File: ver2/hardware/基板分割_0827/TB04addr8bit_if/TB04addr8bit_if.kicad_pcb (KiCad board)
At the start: 2 copper layers, 295 x 195 mm, 307 parts, among them IC201 74HC161N, IC202 74HC161N, IC203 74HC161N, IC204 74HC161N, IC301 74HC161N, IC302 74HC161N, IC303 74HC161N, IC304 74HC161N, IC401 74HC161N, IC402 74HC161N, IC601 74HC161N, J1001 Conn_01x06_Socket, J1002 Conn_01x06_Socket, J1003 Conn_01x06_Socket, J1004 Conn_01x06_Socket, J101 USB_C_Receptacle_PowerOnly_6P, J601 Conn_02x05_Odd_Even, J801 Conn_02x05_Odd_Even, J802 Conn_02x05_Odd_Even, J803 Conn_02x05_Odd_Even, J804 Conn_02x05_Odd_Even, J805 Conn_02x05_Odd_Even, J806 Conn_02x05_Odd_Even, J807 Conn_02x05_Odd_Even, J808 Conn_02x05_Odd_Even, J901 Conn_02x05_Odd_Even, J902 Conn_02x05_Odd_Even, J903 Conn_02x05_Odd_Even, J904 Conn_02x05_Odd_Even, SW1001 SW_DIP_x04, SW1002 SW_DIP_x04, SW1003 SW_DIP_x04, SW1004 SW_DIP_x04, SW101 SW_SPDT, SW501 SW_Push, SW502 sw rotary, SW503 SW_Push, SW601 SW_Coded_SH-7050, U1001 74HC244, U1002 74HC244, U1003 74HC244, U1004 74HC244, U101 74LS157, U102 74HC138, U1101 6116, U1102 74HC244, U1103 74HC244, U1201 74HC193, U1301 74LS08, U1401 74HC138, U1402 74HC244, U1403 74HC244, U1404 74HC244, U1405 74HC244, U1406 74LS157, U1407 74LS139, U1501 74AHC04, U1503 74LS08, U1504 74HC00, U1505 74LS00, U1506 74LS32, U1507 74LS08, U1509 74LS10, U201 74LS253, U202 74LS253, U203 74LS253, U204 74LS253, U301 74LS253, U302 74LS253, U303 74LS253, U304 74LS253, U401 74LS157, U402 74LS253, U403 74LS253, U404 74LS157, U405 74LS253, U406 74LS253, U501 74HC14, U502 4060, U601 74LS273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

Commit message: ver2: 3分割のフットプリント設定完了・取付穴を追加・PCBを作り直し
- 新規コネクタ11件のフットプリントを設定(2x20/2x10ピンソケット・端子台)
- 演算板/制御板/キャリアに取付穴MountingHole_Pad×4とGNDを追加(M3・パッド付きビア)
- 3枚のPCBをコピー元マスターのレイアウトを一掃して作り直し(配置前・配線0)
- 階層から外れて残っていたRS00/RS01.kicad_sch(制御板・IF板)を削除

検証: フットプリント未設定0件、回路図とPCBの参照番号の集合差分0
(演算102/制御101/IF127/キャリア14)、回路図の電気的変更なし

Co-Authored-By: Claude Opus 5 <noreply@anthropic.com>
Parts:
- removed C101, C102, C1101, C1102, C1103, C1201, C1301, C1401, C1402, C1403, C1404, C1407, C1408, C1409, C1501, C1502, C1503, C1504, C1505, C1506, C1507, C201, C202, C203, C204, C205, C206, C207, C208, C301, C302, C303, C304, C305, C306, C307, C308, C401, C402, C403, C404, C405, C406, C407, C408, C601, C602, C603, C604, C605, C606, C607, C608, C701, C702, C703, C704, C705, C706: 0.1u, Capacitor_THT:C_Disc_D4.3mm_W1.9mm_P5.00mm
- removed D1201, D1202, D1203, D201, D202, D203, D204, D205, D206, D207, D208, D209, D210, D211, D212, D213, D214, D215, D216, D301, D302, D303, D304, D305, D306, D307, D308, D309, D310, D311, D312, D313, D314, D315, D316, D601, D602, D603, D604, D605, D606: LED, LED_THT:LED_D3.0mm_Clear
- removed IC201, IC202, IC203, IC204, IC301, IC302, IC303, IC304, IC401, IC402, IC601: 74HC161N, Package_DIP:DIP-16_W7.62mm_Socket
- removed J601, J801, J802, J803, J804, J805, J806, J807, J808: Conn_02x05_Odd_Even, Connector_PinSocket_2.54mm:PinSocket_2x05_P2.54mm_Vertical
- removed R1201, R1202, R1203: 4.7K, Resistor_THT:R_Axial_DIN0207_L6.3mm_D2.5mm_P10.16mm_Horizontal
- removed R601, R602: 3.3K, Resistor_THT:R_Axial_DIN0207_L6.3mm_D2.5mm_P7.62mm_Horizontal
- removed R603, R604, R605, R606: 10K, Resistor_THT:R_Axial_DIN0207_L6.3mm_D2.5mm_P10.16mm_Horizontal
- removed RN201, RN202, RN301, RN302: 4.7K, Resistor_THT:R_Array_SIP9
- removed RN601: 4.7K, Resistor_THT:R_Array_SIP5
- removed SW601: SW_Coded_SH-7050, Library:dip_rotary_sw
- removed U101, U1406, U401, U404: 74LS157, Package_DIP:DIP-16_W7.62mm_Socket
- removed U102, U1401: 74HC138, Package_DIP:DIP-16_W7.62mm_Socket
- removed U1101: 6116, Package_DIP:DIP-24_18.0mmx34.29mm_W15.24mm_Socket
- removed U1102, U1103, U1402, U1403, U1404, U1405: 74HC244, Package_DIP:DIP-20_W7.62mm_Socket
- removed U1201: 74HC193, Package_DIP:DIP-16_W7.62mm_Socket
- removed U1301, U1503, U1507: 74LS08, Package_DIP:DIP-14_W7.62mm_Socket
- removed U1407: 74LS139, Package_DIP:DIP-16_W7.62mm_Socket
- removed U1501: 74AHC04, Package_DIP:DIP-14_W7.62mm_Socket
- removed U1504: 74HC00, Package_DIP:DIP-14_W7.62mm_Socket
- removed U1505: 74LS00, Package_DIP:DIP-14_W7.62mm_Socket
- removed U1506: 74LS32, Package_DIP:DIP-14_W7.62mm_Socket
- removed U1509: 74LS10, Package_DIP:DIP-14_W7.62mm_Socket
- removed U201, U202, U203, U204, U301, U302, U303, U304, U402, U403, U405, U406: 74LS253, Package_DIP:DIP-16_W7.62mm_Socket
- removed U601, U701, U702, U705: 74LS273, Package_DIP:DIP-20_W7.62mm_Socket
- removed U602, U606: 74HC273, Package_DIP:DIP-20_W7.62mm_Socket
- removed U603, U703, U704, U706: 28C256, Package_DIP:DIP-28_W15.24mm_Socket
- removed U604: 28C256, Socket:DIP_Socket-28_W11.9mm_W12.7mm_W15.24mm_W17.78mm_W18.5mm_3M_228-1277-00-0602J
- removed U605: 74HC74, Package_DIP:DIP-14_W7.62mm_Socket
- removed U607: 74HC238, Package_DIP:DIP-16_W7.62mm_Socket
- added J1: Conn_02x20_Odd_Even, Connector_PinSocket_2.54mm:PinSocket_2x20_P2.54mm_Vertical, F.Cu at (28.5, 58.9)
- added J1602: Screw_Terminal_01x02, TerminalBlock:TerminalBlock_MaiXu_MX126-5.0-02P_1x02_P5.00mm, F.Cu at (34.8, 97.2)
- added J4: Conn_02x10_Odd_Even, Connector_PinSocket_2.54mm:PinSocket_2x10_P2.54mm_Vertical, F.Cu at (35.6, 58.9)
- moved H501 420.8 mm to (-66.7, 67.8)
- moved H504 407.6 mm to (-66.7, 91.7)
- moved R502 377.4 mm to (-39.5, 75.5)
- moved R511 376.3 mm to (-39.5, 91.7)
- moved H503 373.4 mm to (-66.7, 83.7)
- moved R510 368.9 mm to (-26.2, 111.1)
- moved H502 368.0 mm to (-66.7, 75.8)
- moved R509 366.5 mm to (-26.2, 107.0)
- moved R501 366.0 mm to (-39.5, 71.5)
- moved SW501 365.5 mm to (-39.6, 99.7)
- moved R506 364.7 mm to (-39.5, 87.7)
- moved R1002 363.1 mm to (-47.4, 2.18)
- moved C501 361.1 mm to (-46.6, 104.5)
- moved C506 359.0 mm to (-3.68, 105.0)
- moved R507 358.0 mm to (-26.2, 99.0)
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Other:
- board size 295 x 195 mm -> 110 x 135 mm

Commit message: ver2: キャリア基板のPCBが完成(査収済み)／IF板の取付穴を配置
キャリア(TB04_carry):
- 外形100x30・角R4、取付穴を四隅に配置
- 表示ソケットJ3-J6は25mmピッチで板の中心に一致
- トラック109本・ビア51個(幅0.20mm/0.80mm)、GNDベタを両面

査収(pcbnew APIで実測):
- DRC 違反0・未配線0
- 全14部品が外形の内側(最小余裕0.70mm)
- 7segIF実測23.05x41.55mm、4台で幅約98mm=100mm板に左右1mmずつ収まる

IF板: 取付穴H501/H502を外形内へ移動(作業中)

Co-Authored-By: Claude Opus 5 <noreply@anthropic.com>
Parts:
- moved H503 288.2 mm to (205.0, 180.0)
- moved H504 274.2 mm to (205.0, 55.0)
- moved H502 200.8 mm to (105.0, 180.0)
- moved H501 172.2 mm to (105.0, 55.0)
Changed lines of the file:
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@@
 	(footprint "MountingHole:MountingHole_3.2mm_M3_Pad_Via"
 		(layer "F.Cu")
-		(at -66.697056 67.847056)
+		(at 105 55)
 		(descr "Mounting Hole 3.2mm, M3, generated by kicad-footprint-generator mountinghole.py")
 		(tags "mountinghole M3")
@@
 	(footprint "MountingHole:MountingHole_3.2mm_M3_Pad_Via"
 		(layer "F.Cu")
-		(at -66.697056 75.797056)
+		(at 105 180)
 		(descr "Mounting Hole 3.2mm, M3, generated by kicad-footprint-generator mountinghole.py")
 		(tags "mountinghole M3")
@@
 		(tags "CP Radial series Radial pin pitch 2.00mm diameter 5mm height 7mm Electrolytic Capacitor")
 		(property "Reference" "C501"
-			(at -20.677056 -9.302944 0)
+			(at 1 -2.75 0)
 			(layer "F.SilkS")
 			(effects
@@
 	(footprint "MountingHole:MountingHole_3.2mm_M3_Pad_Via"
 		(layer "F.Cu")
-		(at -66.697056 83.747056)
+		(at 205 180)
 		(descr "Mounting Hole 3.2mm, M3, generated by kicad-footprint-generator mountinghole.py")
 		(tags "mountinghole M3")
@@
 	(footprint "MountingHole:MountingHole_3.2mm_M3_Pad_Via"
 		(layer "F.Cu")
-		(at -66.697056 91.697056)
+		(at 205 55)
 		(descr "Mounting Hole 3.2mm, M3, generated by kicad-footprint-generator mountinghole.py")
 		(tags "mountinghole M3")

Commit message: ver2: デザインルールを3枚へコピー／制御板の配置を決定(200x180へ拡大)
デザインルール(キャリアで決めた値を_ctrl/_alu/_ifへ):
- 信号0.2mm・電源0.8mm・クリアランス0.2mm・ビア0.6/0.3
- 銅箔-基板端0.5mm、ゾーン最小クリアランス0.5mm

制御板の配置:
- 200x135では部品が55mm分あふれるため200x180へ拡大($16.9->$21.3)
- ブロックの左右はケーブルの向きで決定(J1=IF板/J2,J3=演算板への
  接続本数の差で並べ、ROM_ALUを演算板側の右端へ)
- 並び: ram,addrMUX -> PC_aluMux,sp,addrDecord -> gates -> Decoder -> ROM_ALU
- パスコンは全34ICの1番ピンと電源ピンの間(DIPの上辺)に配置
- 表示8桁を下端に25mmピッチ一列、ケーブルは左右端、電源入口は上端

検証: 外形はみ出し0・courtyard重なり0・パスコン34/34
DRC違反はシルク3件のみ(未配線499は配線前のため)

同梱: 並行して行われた回路図編集(キャリア用2x10を廃し2x5直挿しへ。
制御板はJ5削除、IF板はJ4->J10-J13)

Co-Authored-By: Claude Opus 5 <noreply@anthropic.com>
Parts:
- removed J4: Conn_02x10_Odd_Even, Connector_PinSocket_2.54mm:PinSocket_2x10_P2.54mm_Vertical
- added J10: Conn_02x05_Odd_Even, Connector_PinSocket_2.54mm:PinSocket_2x05_P2.54mm_Vertical, F.Cu at (113.3, 134.8)
- added J11: Conn_02x05_Odd_Even, Connector_PinSocket_2.54mm:PinSocket_2x05_P2.54mm_Vertical, F.Cu at (120.5, 134.8)
- added J12: Conn_02x05_Odd_Even, Connector_PinSocket_2.54mm:PinSocket_2x05_P2.54mm_Vertical, F.Cu at (127.6, 134.8)
- added J13: Conn_02x05_Odd_Even, Connector_PinSocket_2.54mm:PinSocket_2x05_P2.54mm_Vertical, F.Cu at (134.7, 134.8)
- U901, U902, U903, U905: value 74LS377 -> 74HC377

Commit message: ver2: IF板PCBの孤立フットプリント3個を削除(回路図と110部品で一致)
RN1003/RN1005/RN1007を「回路図からPCBを更新」で除去。
回路図側の差分はuuid行のみで電気的変更なし。

Co-Authored-By: Claude Opus 5 <noreply@anthropic.com>
Claude-Session: https://claude.ai/code/session_01AfeTYjKzCvUCekJLNec6bd
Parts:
- removed R1001, R1002, R1003, R1004, R1005, R1006, R1007, R1008, R1009, R1010, R1011, R1012, R1013, R1014, R1015, R1016: 1K, Resistor_THT:R_Axial_DIN0207_L6.3mm_D2.5mm_P10.16mm_Horizontal
- removed RN1003, RN1005, RN1007, RN903, RN904: 4.7K, Resistor_THT:R_Array_SIP5
- added RN1001: 4.7K, Resistor_THT:R_Array_SIP9, F.Cu at (134.7, 157.0)
- RN1002, RN901, RN902: footprint Resistor_THT:R_Array_SIP5 -> Resistor_THT:R_Array_SIP9
- RN1009, RN1010: value 47K -> 10K
- moved R501 279.2 mm to (237.1, 109.6)
- moved R502 279.2 mm to (237.1, 113.6)
- moved R503 279.2 mm to (237.1, 117.7)
- moved R505 279.2 mm to (237.1, 121.7)
- moved R506 279.2 mm to (237.1, 125.8)
- moved R511 279.2 mm to (237.1, 129.8)
- moved R512 279.2 mm to (237.1, 133.9)
- moved SW502 279.2 mm to (258.5, 119.3)
- moved U501 279.2 mm to (261.7, 133.1)
- moved C501 279.2 mm to (229.9, 142.6)
- moved C502 279.2 mm to (229.9, 149.2)
- moved C503 279.2 mm to (272.9, 132.7)
- moved C504 279.2 mm to (272.9, 136.2)
- moved C505 279.2 mm to (272.9, 139.6)
- moved C506 279.2 mm to (272.9, 143.1)
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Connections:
- RN1002 pad 2: Net-(D1004-K) -> Net-(D1009-K)
- RN1002 pad 3: Net-(D1002-K) -> Net-(D1010-K)
- RN1002 pad 4: Net-(D1003-K) -> Net-(D1011-K)
- RN1002 pad 5: Net-(D1001-K) -> Net-(D1012-K)
- RN901 pad 2: Net-(D904-K) -> Net-(D901-K)
- RN901 pad 3: Net-(D902-K) -> Net-(D903-K)
- RN901 pad 4: Net-(D903-K) -> Net-(D902-K)
- RN901 pad 5: Net-(D901-K) -> Net-(D904-K)
- RN902 pad 2: Net-(D908-K) -> Net-(D909-K)
- RN902 pad 3: Net-(D907-K) -> Net-(D910-K)
- RN902 pad 4: Net-(D906-K) -> Net-(D911-K)
- RN902 pad 5: Net-(D905-K) -> Net-(D912-K)
- SW1001 pad 5: Net-(R1008-Pad2) -> VDD
- SW1001 pad 6: Net-(R1007-Pad2) -> VDD
- SW1001 pad 7: Net-(R1006-Pad2) -> VDD
- SW1001 pad 8: Net-(R1005-Pad2) -> VDD
- SW1002 pad 5: Net-(R1012-Pad2) -> VDD
- SW1002 pad 6: Net-(R1011-Pad2) -> VDD
- SW1002 pad 7: Net-(R1010-Pad2) -> VDD
- SW1002 pad 8: Net-(R1009-Pad2) -> VDD
- SW1003 pad 5: Net-(R1016-Pad2) -> VDD
- SW1003 pad 6: Net-(R1015-Pad2) -> VDD
- SW1003 pad 7: Net-(R1014-Pad2) -> VDD
- SW1003 pad 8: Net-(R1013-Pad2) -> VDD
- SW1004 pad 5: Net-(R1004-Pad2) -> VDD
- SW1004 pad 6: Net-(R1003-Pad2) -> VDD
- SW1004 pad 7: Net-(R1002-Pad2) -> VDD
- SW1004 pad 8: Net-(R1001-Pad2) -> VDD

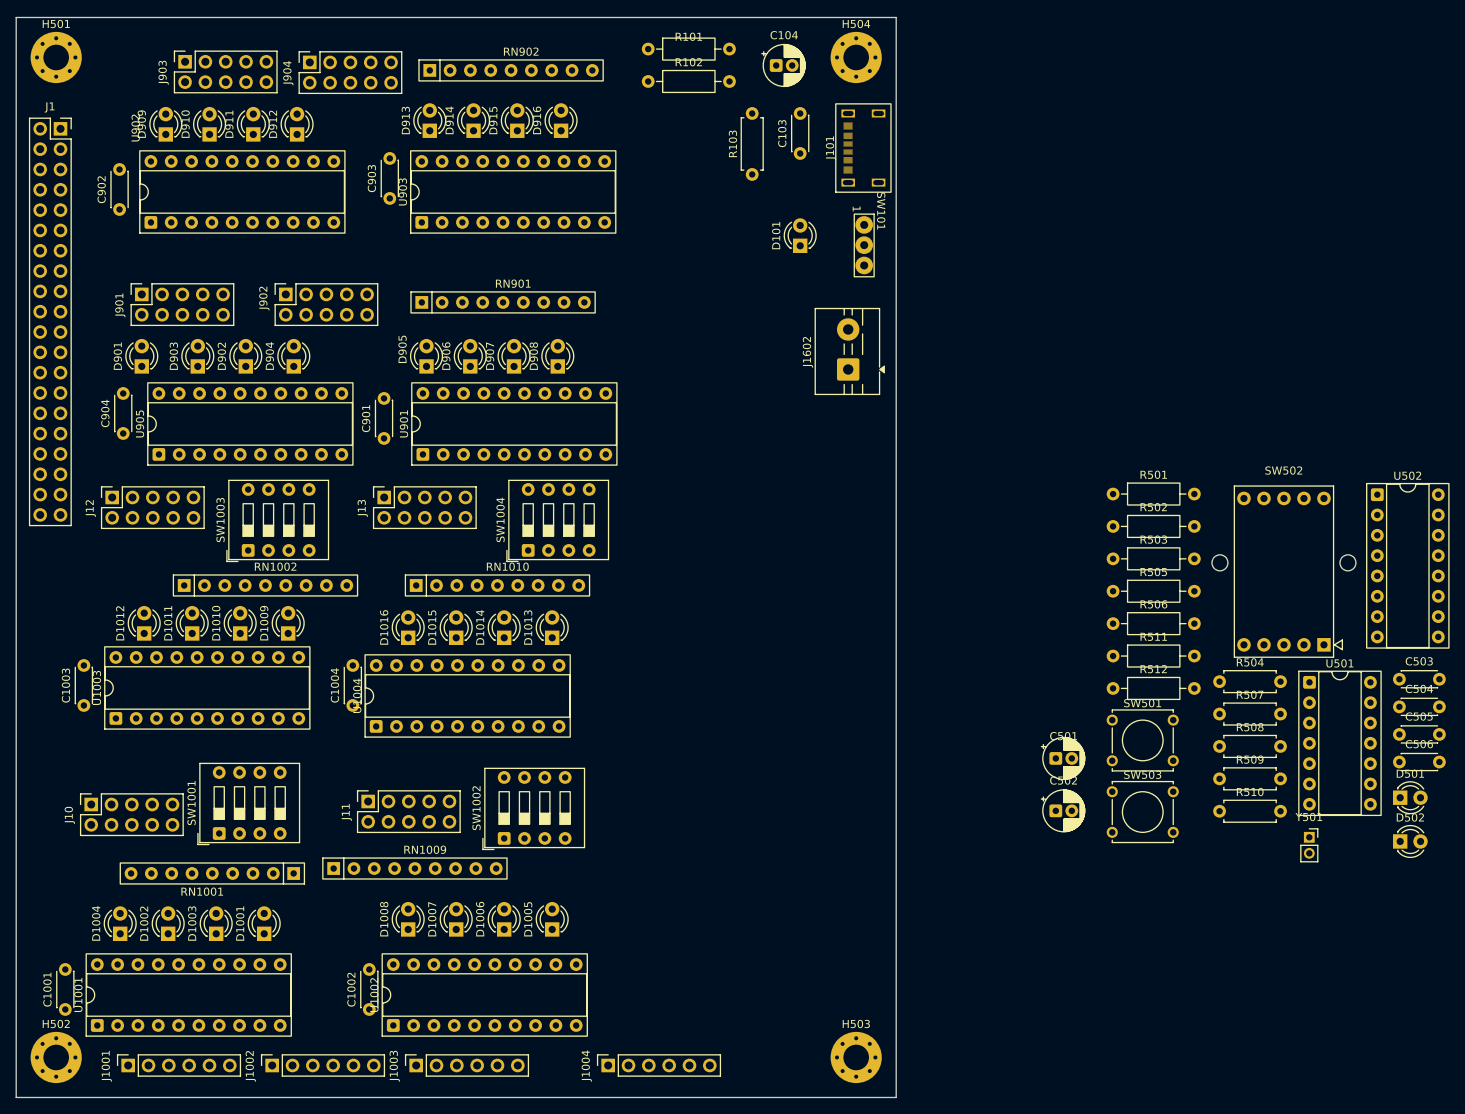
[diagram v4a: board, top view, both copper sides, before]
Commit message: ver2: IF板の部品を粗配置(INPUT表示用7segIFコネクタJ10-J13を配置・未決定)
パッドはみ出し0・courtyard重なり1組。
7segIFモジュール8台は空中で11組干渉するため配置は要検討。

Co-Authored-By: Claude Opus 5 <noreply@anthropic.com>
Claude-Session: https://claude.ai/code/session_01AfeTYjKzCvUCekJLNec6bd
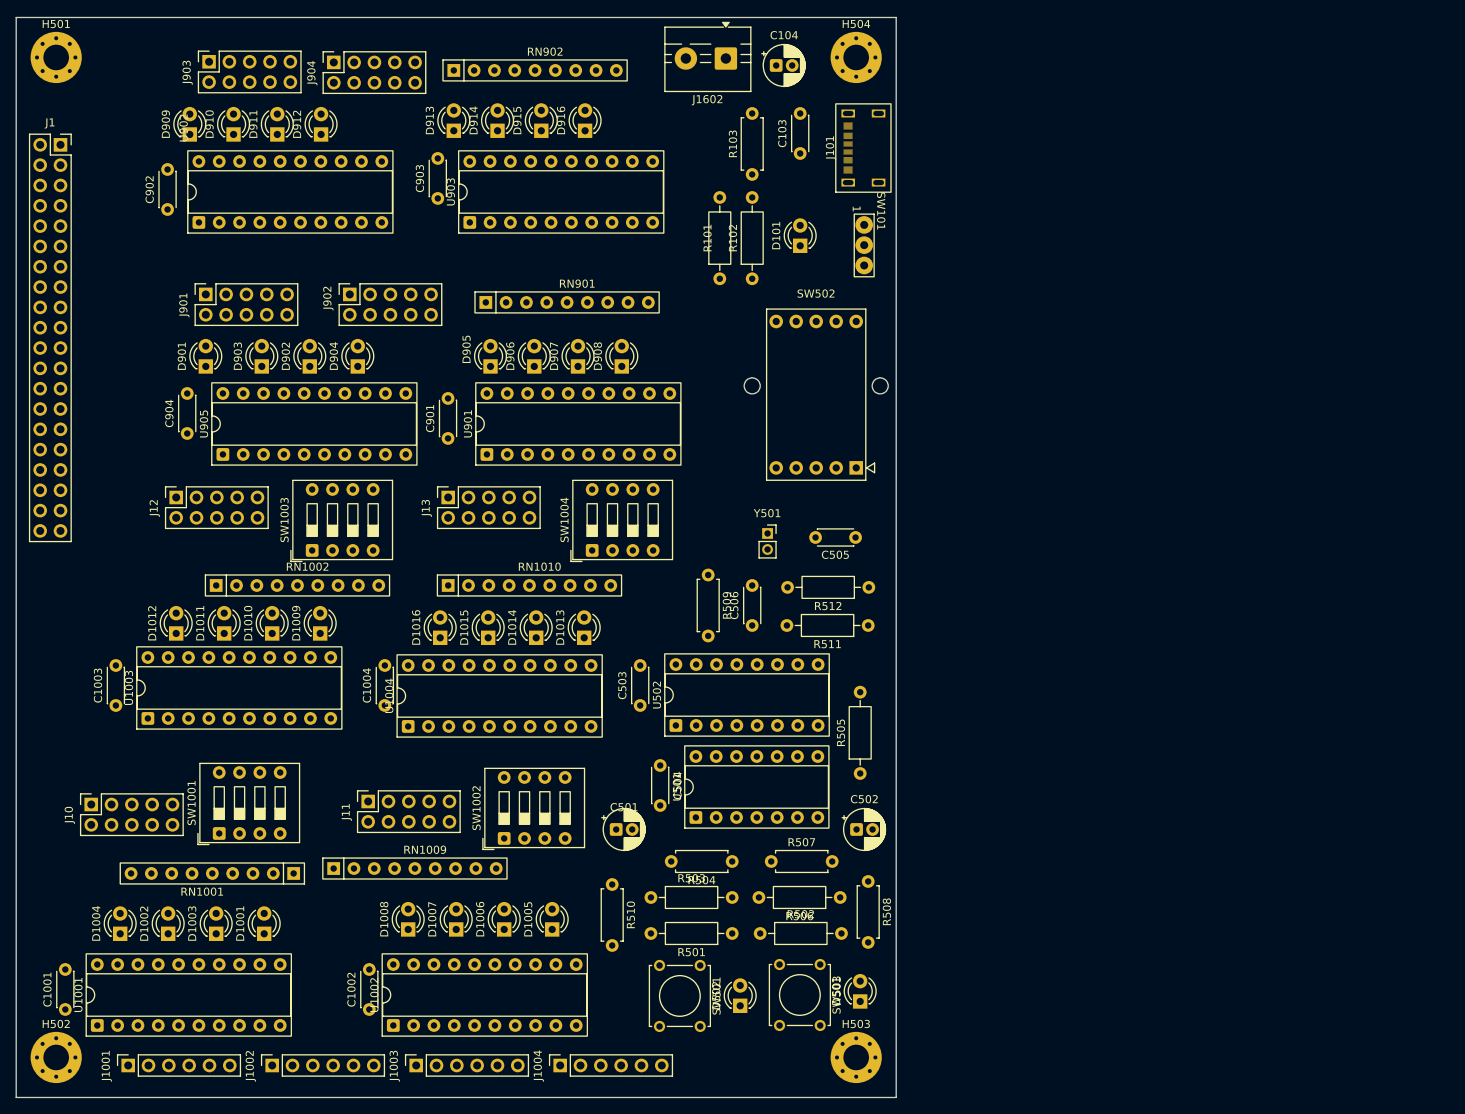
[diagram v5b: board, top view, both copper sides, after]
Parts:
- moved C503 95.0 mm to (178.0, 136.0), turned to 90 degrees
- moved C504 92.7 mm to (180.5, 143.5), turned to -90 degrees
- moved U502 92.3 mm to (182.5, 138.5), turned to 90 degrees
- moved D502 85.0 mm to (190.5, 173.5), turned to 90 degrees
- moved C506 82.7 mm to (192.0, 126.0), turned to 90 degrees
- moved U501 78.5 mm to (185.0, 150.0), turned to 90 degrees
- moved Y501 77.6 mm to (193.9, 114.5)
- moved R510 76.5 mm to (174.5, 158.4), turned to -90 degrees
- moved R501 72.7 mm to (189.5, 164.5), turned to 180 degrees
- moved C505 72.3 mm to (204.9, 115.0), turned to 180 degrees
- moved D501 72.1 mm to (205.5, 173.0), turned to 90 degrees
- moved R503 71.6 mm to (179.3, 160.0)
- moved R509 68.8 mm to (186.5, 119.7), turned to -90 degrees
- moved R502 67.3 mm to (193.0, 164.5)
- moved R504 64.9 mm to (189.5, 155.5), turned to 180 degrees
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
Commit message: ver2: IF板の7segIFソケット間隔を確保する配置に更新
基板同士の隙間は10.62〜20.89mm(基準10mm)。
垂直実装(L字ピンヘッダ)・基板幅24mm・ソケットからの左右はみ出し5mm。

Co-Authored-By: Claude Opus 5 <noreply@anthropic.com>
Claude-Session: https://claude.ai/code/session_01AfeTYjKzCvUCekJLNec6bd
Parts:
- moved RN901 23.7 mm to (135.0, 85.0)
- moved J904 22.4 mm to (162.0, 54.0)
- moved J902 21.1 mm to (162.8, 84.0)
- moved RN902 19.7 mm to (135.0, 57.0)
- moved J903 7.00 mm to (117.1, 55.5)
- moved J901 5.73 mm to (118.0, 84.0)
- moved J12 3.00 mm to (117.0, 110.0)
- moved SW1004 3.00 mm to (175.0, 116.6)
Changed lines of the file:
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@@
 	(footprint "Connector_PinSocket_2.54mm:PinSocket_2x05_P2.54mm_Vertical"
 		(layer "F.Cu")
-		(at 139.7 55.62 90)
+		(at 162 54 90)
 		(descr "Through hole straight socket strip, 2x05, 2.54mm pitch, double rows (from Kicad 4.0.7), script generated")
 		(tags "Through hole socket strip THT 2x05 2.54mm double row")
@@
 	(footprint "Connector_PinSocket_2.54mm:PinSocket_2x05_P2.54mm_Vertical"
 		(layer "F.Cu")
-		(at 141.7 84.62 90)
+		(at 162.787486 83.963983 90)
 		(descr "Through hole straight socket strip, 2x05, 2.54mm pitch, double rows (from Kicad 4.0.7), script generated")
 		(tags "Through hole socket strip THT 2x05 2.54mm double row")
@@
 	(footprint "Resistor_THT:R_Array_SIP9"
 		(layer "F.Cu")
-		(at 154.7 56.62)
+		(at 135 57)
 		(descr "9-pin Resistor SIP pack")
 		(tags "R")
@@
 	(footprint "Connector_PinSocket_2.54mm:PinSocket_2x05_P2.54mm_Vertical"
 		(layer "F.Cu")
-		(at 124.11 55.54 90)
+		(at 117.11 55.54 90)
 		(descr "Through hole straight socket strip, 2x05, 2.54mm pitch, double rows (from Kicad 4.0.7), script generated")
 		(tags "Through hole socket strip THT 2x05 2.54mm double row")
@@
 	(footprint "Button_Switch_THT:SW_DIP_SPSTx04_Slide_9.78x12.34mm_W7.62mm_P2.54mm"
 		(layer "F.Cu")
-		(at 172 116.62 90)
+		(at 175 116.62 90)
 		(descr "4x-dip-switch SPST , Slide, row spacing 7.62 mm (300 mils), body size 9.78x12.34mm (see e.g. https://www.ctscorp.com/wp-content/uploads/206-208.pdf)")
 		(tags "DIP Switch SPST Slide 7.62mm 300mil")
@@
 		)
 		(point
-			(at 175.81 112.81)
+			(at 178.81 112.81)
 			(size 1.27)
 			(layer "F.Fab")
@@
 	(footprint "Connector_PinSocket_2.54mm:PinSocket_2x05_P2.54mm_Vertical"
 		(layer "F.Cu")
-		(at 123.7 84.62 90)
+		(at 118 84 90)
 		(descr "Through hole straight socket strip, 2x05, 2.54mm pitch, double rows (from Kicad 4.0.7), script generated")
 		(tags "Through hole socket strip THT 2x05 2.54mm double row")
@@
 	(footprint "Resistor_THT:R_Array_SIP9"
 		(layer "F.Cu")
-		(at 158.7 85.62)
+		(at 135 85)
 		(descr "9-pin Resistor SIP pack")
 		(tags "R")
@@
 	(footprint "Connector_PinSocket_2.54mm:PinSocket_2x05_P2.54mm_Vertical"
 		(layer "F.Cu")
-		(at 120 110 90)
+		(at 117 110 90)
 		(descr "Through hole straight socket strip, 2x05, 2.54mm pitch, double rows (from Kicad 4.0.7), script generated")
 		(tags "Through hole socket strip THT 2x05 2.54mm double row")
